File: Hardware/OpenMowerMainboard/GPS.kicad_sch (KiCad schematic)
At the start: 3 parts, among them U7 SIP32509DT

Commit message: added footprints to schematic
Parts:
- JP1: footprint (none) -> Jumper:SolderJumper-3_P1.3mm_Bridged12_Pad1.0x1.5mm
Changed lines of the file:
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@@
     (property "Reference" "JP1" (id 0) (at 212.09 113.03 0))
     (property "Value" "SolderJumper_3_Bridged12" (id 1) (at 212.09 115.57 0))
-    (property "Footprint" "" (id 2) (at 212.09 109.22 0)
+    (property "Footprint" "Jumper:SolderJumper-3_P1.3mm_Bridged12_Pad1.0x1.5mm" (id 2) (at 212.09 109.22 0)
       (effects (font (size 1.27 1.27)) hide)
     )

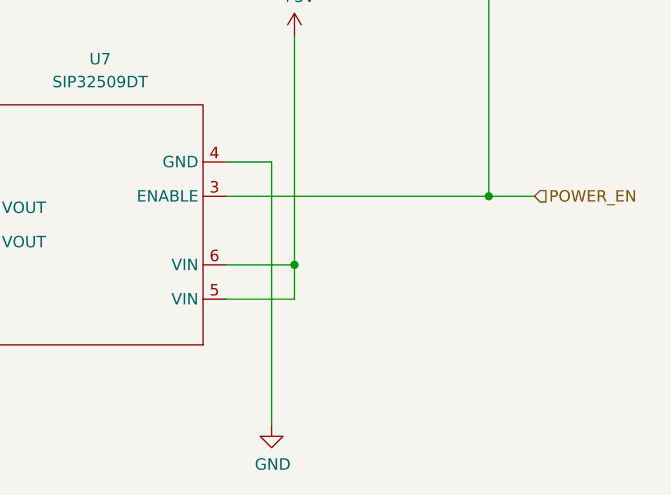
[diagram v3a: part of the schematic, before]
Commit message: Added default pull down, raspberry pi power override and some TODOs
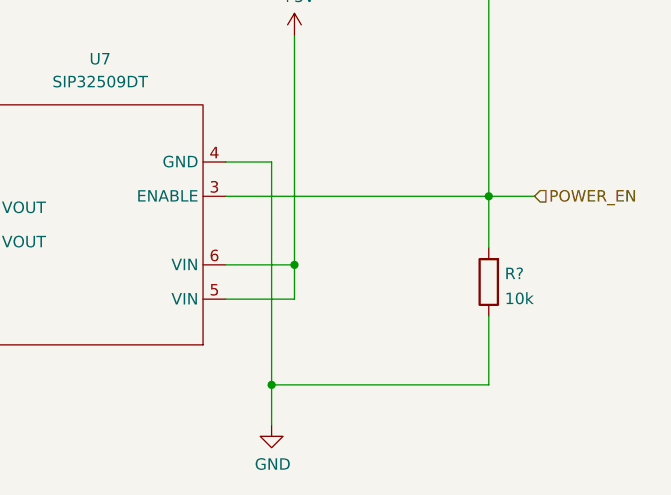
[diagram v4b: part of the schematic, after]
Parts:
- added R?: 10k, Resistor_SMD:R_0805_2012Metric_Pad1.20x1.40mm_HandSolder, symbol Device:R
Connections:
- net GND: now also R?.1
- net POWER_EN: now also R?.2
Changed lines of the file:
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@@
   (junction (at 118.11 93.98) (diameter 0) (color 0 0 0 0)
+  )
+  (junction (at 194.31 161.925) (diameter 0) (color 0 0 0 0)
   )
   (no_connect (at 121.92 83.82))
@@
     (stroke (width 0) (type default) (color 0 0 0 0))
   )
+  (wire (pts (xy 218.44 140.97) (xy 218.44 146.685))
+    (stroke (width 0) (type default) (color 0 0 0 0))
+  )
   (wire (pts (xy 201.93 109.22) (xy 207.01 109.22))
     (stroke (width 0) (type default) (color 0 0 0 0))
   )
+  (wire (pts (xy 218.44 154.305) (xy 218.44 161.925))
+    (stroke (width 0) (type default) (color 0 0 0 0))
+  )
   (wire (pts (xy 189.23 140.97) (xy 218.44 140.97))
     (stroke (width 0) (type default) (color 0 0 0 0))
@@
     (stroke (width 0) (type default) (color 0 0 0 0))
   )
+  (wire (pts (xy 218.44 161.925) (xy 194.31 161.925))
+    (stroke (width 0) (type default) (color 0 0 0 0))
+  )
   (wire (pts (xy 118.11 91.44) (xy 118.11 93.98))
     (stroke (width 0) (type default) (color 0 0 0 0))
@@
     (stroke (width 0) (type default) (color 0 0 0 0))
   )
-  (wire (pts (xy 194.31 137.16) (xy 194.31 166.37))
+  (wire (pts (xy 194.31 137.16) (xy 194.31 161.925))
     (stroke (width 0) (type default) (color 0 0 0 0))
   )
@@
   )
   (wire (pts (xy 187.96 104.14) (xy 212.09 104.14))
+    (stroke (width 0) (type default) (color 0 0 0 0))
+  )
+  (wire (pts (xy 194.31 161.925) (xy 194.31 166.37))
     (stroke (width 0) (type default) (color 0 0 0 0))
   )
@@
     (pin "3")
   )
+  (symbol (lib_id "Device:R") (at 218.44 150.495 180) (unit 1)
+    (in_bom yes) (on_board yes) (fields_autoplaced)
+    (property "Reference" "R?" (id 0) (at 220.218 149.5865 0)
+      (effects (font (size 1.27 1.27)) (justify right))
+    )
+    (property "Value" "10k" (id 1) (at 220.218 152.3616 0)
+      (effects (font (size 1.27 1.27)) (justify right))
+    )
+    (property "Footprint" "Resistor_SMD:R_0805_2012Metric_Pad1.20x1.40mm_HandSolder" (id 2) (at 220.218 150.495 90)
+      (effects (font (size 1.27 1.27)) hide)
+    )
+    (property "Datasheet" "~" (id 3) (at 218.44 150.495 0)
+      (effects (font (size 1.27 1.27)) hide)
+    )
+    (pin "1")
+    (pin "2")
+  )
   (symbol (lib_id "power:+3.3V") (at 201.93 109.22 0) (unit 1)

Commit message: WIP hardware revision
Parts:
- removed JP1: SolderJumper_3_Bridged12, Jumper:SolderJumper-3_P1.3mm_Bridged12_Pad1.0x1.5mm, symbol Jumper:SolderJumper_3_Bridged12
- removed R?: 10k, Resistor_SMD:R_0805_2012Metric_Pad1.20x1.40mm_HandSolder, symbol Device:R
- removed U7: SIP32509DT, Package_TO_SOT_SMD:SOT-23-6_Handsoldering, symbol OpenMowerMainboardLib:SIP32509DT
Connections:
- net GPS_POWER is gone; now on net +5V: XA1.5V1 (5V)
- net +3V3: now also XA1.IORF (IOREF)
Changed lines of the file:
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@@
 (kicad_sch (version 20211123) (generator eeschema)
   (paper "A4")
-  (junction (at 157.48 142.24) (diameter 0) (color 0 0 0 0)
-  )
-  (junction (at 218.44 140.97) (diameter 0) (color 0 0 0 0)
-  )
   (junction (at 118.11 96.52) (diameter 0) (color 0 0 0 0)
   )
-  (junction (at 196.85 148.59) (diameter 0) (color 0 0 0 0)
-  )
   (junction (at 118.11 93.98) (diameter 0) (color 0 0 0 0)
-  )
-  (junction (at 194.31 161.925) (diameter 0) (color 0 0 0 0)
   )
   (no_connect (at 121.92 83.82))
@@
     (stroke (width 0) (type default) (color 0 0 0 0))
   )
-  (wire (pts (xy 157.48 142.24) (xy 157.48 146.05))
-    (stroke (width 0) (type default) (color 0 0 0 0))
-  )
-  (wire (pts (xy 218.44 109.22) (xy 218.44 140.97))
-    (stroke (width 0) (type default) (color 0 0 0 0))
-  )
-  (wire (pts (xy 196.85 152.4) (xy 196.85 148.59))
-    (stroke (width 0) (type default) (color 0 0 0 0))
-  )
-  (wire (pts (xy 218.44 109.22) (xy 217.17 109.22))
-    (stroke (width 0) (type default) (color 0 0 0 0))
-  )
-  (wire (pts (xy 218.44 140.97) (xy 218.44 146.685))
-    (stroke (width 0) (type default) (color 0 0 0 0))
-  )
-  (wire (pts (xy 201.93 109.22) (xy 207.01 109.22))
-    (stroke (width 0) (type default) (color 0 0 0 0))
-  )
-  (wire (pts (xy 218.44 154.305) (xy 218.44 161.925))
-    (stroke (width 0) (type default) (color 0 0 0 0))
-  )
-  (wire (pts (xy 189.23 140.97) (xy 218.44 140.97))
-    (stroke (width 0) (type default) (color 0 0 0 0))
-  )
-  (wire (pts (xy 218.44 140.97) (xy 223.52 140.97))
-    (stroke (width 0) (type default) (color 0 0 0 0))
-  )
-  (wire (pts (xy 218.44 161.925) (xy 194.31 161.925))
-    (stroke (width 0) (type default) (color 0 0 0 0))
-  )
   (wire (pts (xy 118.11 91.44) (xy 118.11 93.98))
     (stroke (width 0) (type default) (color 0 0 0 0))
@@
     (stroke (width 0) (type default) (color 0 0 0 0))
   )
-  (wire (pts (xy 157.48 146.05) (xy 161.29 146.05))
+  (wire (pts (xy 96.52 98.425) (xy 96.52 101.6))
     (stroke (width 0) (type default) (color 0 0 0 0))
   )
-  (wire (pts (xy 157.48 142.24) (xy 161.29 142.24))
-    (stroke (width 0) (type default) (color 0 0 0 0))
-  )
-  (wire (pts (xy 99.06 101.6) (xy 121.92 101.6))
+  (wire (pts (xy 96.52 101.6) (xy 121.92 101.6))
     (stroke (width 0) (type default) (color 0 0 0 0))
   )
@@
     (stroke (width 0) (type default) (color 0 0 0 0))
   )
-  (wire (pts (xy 142.24 142.24) (xy 157.48 142.24))
-    (stroke (width 0) (type default) (color 0 0 0 0))
-  )
-  (wire (pts (xy 212.09 104.14) (xy 212.09 105.41))
-    (stroke (width 0) (type default) (color 0 0 0 0))
-  )
   (wire (pts (xy 121.92 91.44) (xy 118.11 91.44))
-    (stroke (width 0) (type default) (color 0 0 0 0))
-  )
-  (wire (pts (xy 189.23 152.4) (xy 196.85 152.4))
     (stroke (width 0) (type default) (color 0 0 0 0))
   )
@@
     (stroke (width 0) (type default) (color 0 0 0 0))
   )
-  (wire (pts (xy 196.85 123.19) (xy 196.85 148.59))
-    (stroke (width 0) (type default) (color 0 0 0 0))
-  )
-  (wire (pts (xy 194.31 137.16) (xy 194.31 161.925))
-    (stroke (width 0) (type default) (color 0 0 0 0))
-  )
-  (wire (pts (xy 189.23 148.59) (xy 196.85 148.59))
-    (stroke (width 0) (type default) (color 0 0 0 0))
-  )
-  (wire (pts (xy 189.23 137.16) (xy 194.31 137.16))
-    (stroke (width 0) (type default) (color 0 0 0 0))
-  )
-  (wire (pts (xy 187.96 104.14) (xy 212.09 104.14))
-    (stroke (width 0) (type default) (color 0 0 0 0))
-  )
-  (wire (pts (xy 194.31 161.925) (xy 194.31 166.37))
+  (wire (pts (xy 187.96 104.14) (xy 196.85 104.14))
     (stroke (width 0) (type default) (color 0 0 0 0))
   )
@@
     (effects (font (size 1.27 1.27)) (justify left bottom))
   )
-  (label "GPS_POWER" (at 142.24 142.24 0)
-    (effects (font (size 1.27 1.27)) (justify left bottom))
-  )
   (hierarchical_label "TXD" (shape output) (at 121.92 50.8 180)
     (effects (font (size 1.27 1.27)) (justify right))
-  )
-  (hierarchical_label "POWER_EN" (shape input) (at 223.52 140.97 0)
-    (effects (font (size 1.27 1.27)) (justify left))
   )
   (hierarchical_label "RXD" (shape input) (at 121.92 53.34 180)
@@
     (pin "VIN")
   )
-  (symbol (lib_id "Jumper:SolderJumper_3_Bridged12") (at 212.09 109.22 180) (unit 1)
+  (symbol (lib_id "power:+3.3V") (at 196.85 104.14 0) (unit 1)
     (in_bom yes) (on_board yes) (fields_autoplaced)
-    (property "Reference" "JP1" (id 0) (at 212.09 113.03 0))
-    (property "Value" "SolderJumper_3_Bridged12" (id 1) (at 212.09 115.57 0))
-    (property "Footprint" "Jumper:SolderJumper-3_P1.3mm_Bridged12_Pad1.0x1.5mm" (id 2) (at 212.09 109.22 0)
+    (property "Reference" "#PWR0116" (id 0) (at 196.85 107.95 0)
       (effects (font (size 1.27 1.27)) hide)
     )
-    (property "Datasheet" "~" (id 3) (at 212.09 109.22 0)
+    (property "Value" "+3.3V" (id 1) (at 196.85 99.06 0))
+    (property "Footprint" "" (id 2) (at 196.85 104.14 0)
       (effects (font (size 1.27 1.27)) hide)
     )
-    (pin "1")
-    (pin "2")
-    (pin "3")
-  )
-  (symbol (lib_id "Device:R") (at 218.44 150.495 180) (unit 1)
-    (in_bom yes) (on_board yes) (fields_autoplaced)
-    (property "Reference" "R?" (id 0) (at 220.218 149.5865 0)
-      (effects (font (size 1.27 1.27)) (justify right))
-    )
-    (property "Value" "10k" (id 1) (at 220.218 152.3616 0)
-      (effects (font (size 1.27 1.27)) (justify right))
-    )
-    (property "Footprint" "Resistor_SMD:R_0805_2012Metric_Pad1.20x1.40mm_HandSolder" (id 2) (at 220.218 150.495 90)
-      (effects (font (size 1.27 1.27)) hide)
-    )
-    (property "Datasheet" "~" (id 3) (at 218.44 150.495 0)
-      (effects (font (size 1.27 1.27)) hide)
-    )
-    (pin "1")
-    (pin "2")
-  )
-  (symbol (lib_id "power:+3.3V") (at 201.93 109.22 0) (unit 1)
-    (in_bom yes) (on_board yes) (fields_autoplaced)
-    (property "Reference" "#PWR0116" (id 0) (at 201.93 113.03 0)
-      (effects (font (size 1.27 1.27)) hide)
-    )
-    (property "Value" "+3.3V" (id 1) (at 201.93 104.14 0))
-    (property "Footprint" "" (id 2) (at 201.93 109.22 0)
-      (effects (font (size 1.27 1.27)) hide)
-    )
-    (property "Datasheet" "" (id 3) (at 201.93 109.22 0)
+    (property "Datasheet" "" (id 3) (at 196.85 104.14 0)
       (effects (font (size 1.27 1.27)) hide)
     )
     (pin "1")
   )
-  (symbol (lib_id "OpenMowerMainboardLib:SIP32509DT") (at 163.83 116.84 180) (unit 1)
-    (in_bom yes) (on_board yes) (fields_autoplaced)
-    (property "Reference" "U7" (id 0) (at 175.26 125.73 0))
-    (property "Value" "SIP32509DT" (id 1) (at 175.26 128.27 0))
-    (property "Footprint" "Package_TO_SOT_SMD:SOT-23-6_Handsoldering" (id 2) (at 163.83 116.84 0)
+  (symbol (lib_id "power:+5V") (at 96.52 98.425 0) (unit 1)
+    (in_bom yes) (on_board yes)
+    (property "Reference" "#PWR0134" (id 0) (at 96.52 102.235 0)
       (effects (font (size 1.27 1.27)) hide)
     )
-    (property "Datasheet" "" (id 3) (at 163.83 116.84 0)
+    (property "Value" "+5V" (id 1) (at 96.901 94.0308 0))
+    (property "Footprint" "" (id 2) (at 96.52 98.425 0)
       (effects (font (size 1.27 1.27)) hide)
     )
-    (pin "1")
-    (pin "2")
-    (pin "3")
-    (pin "4")
-    (pin "5")
-    (pin "6")
-  )
-  (symbol (lib_id "power:+5V") (at 196.85 123.19 0) (unit 1)
-    (in_bom yes) (on_board yes)
-    (property "Reference" "#PWR0134" (id 0) (at 196.85 127 0)
+    (property "Datasheet" "" (id 3) (at 96.52 98.425 0)
       (effects (font (size 1.27 1.27)) hide)
     )
-    (property "Value" "+5V" (id 1) (at 197.231 118.7958 0))
-    (property "Footprint" "" (id 2) (at 196.85 123.19 0)
-      (effects (font (size 1.27 1.27)) hide)
-    )
-    (property "Datasheet" "" (id 3) (at 196.85 123.19 0)
-      (effects (font (size 1.27 1.27)) hide)
-    )
-    (pin "1")
-  )
-  (symbol (lib_id "power:GND") (at 194.31 166.37 0) (unit 1)
-    (in_bom yes) (on_board yes)
-    (property "Reference" "#PWR0133" (id 0) (at 194.31 172.72 0)
-      (effects (font (size 1.27 1.27)) hide)
-    )
-    (property "Value" "GND" (id 1) (at 194.437 170.7642 0))
-    (property "Footprint" "" (id 2) (at 194.31 166.37 0)
-      (effects (font (size 1.27 1.27)) hide)
-    )
-    (property "Datasheet" "" (id 3) (at 194.31 166.37 0)
-      (effects (font (size 1.27 1.27)) hide)
-    )

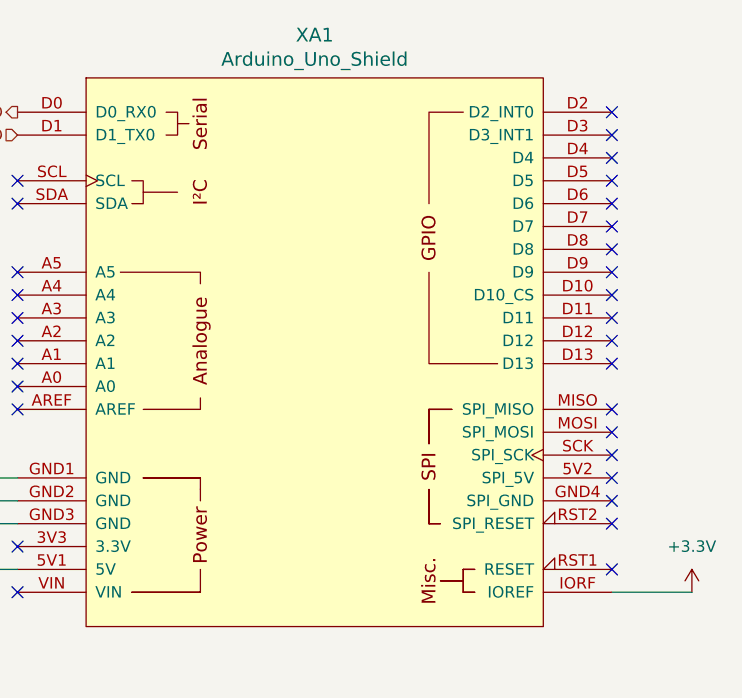
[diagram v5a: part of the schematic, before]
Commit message: v0_9_1 mainboard rework
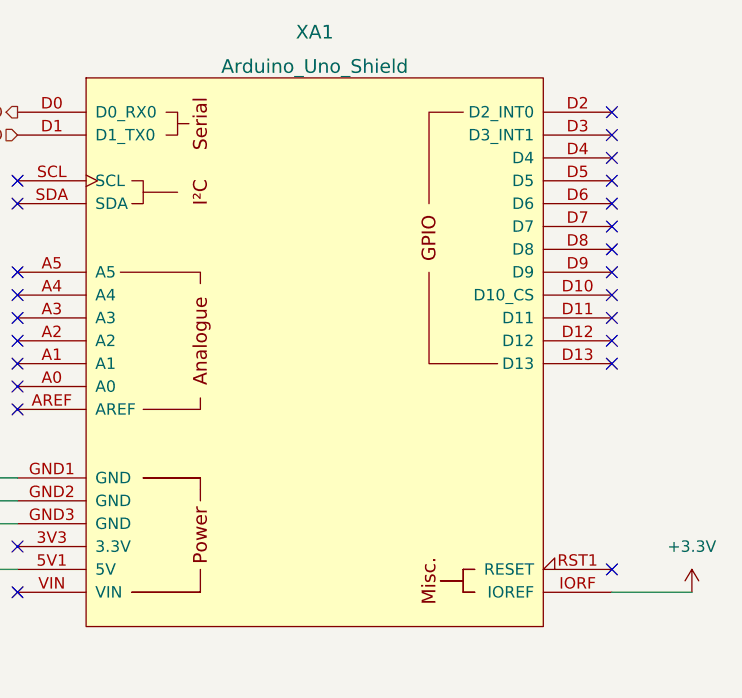
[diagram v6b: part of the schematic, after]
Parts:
- removed XA1: Arduino_Uno_Shield, Arduino:Arduino_Uno_Shield, symbol arduino:Arduino_Uno_Shield
- added XA1: Arduino_Uno_Shield, MyModules:Arduino_Uno_Shield, symbol MyModules:Arduino_Uno_Shield
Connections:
- net +3V3: now also XA1.IORF (IOREF)
- net +5V: now also XA1.5V1 (5V)
- net GND: now also XA1.GND1 (GND), XA1.GND2 (GND), XA1.GND3 (GND)
- net RXD: now also XA1.D1 (D1_TX0)
- net TXD: now also XA1.D0 (D0_RX0)
- no-connect marks 30 -> 24
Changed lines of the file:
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@@
   (no_connect (at 187.96 76.2))
   (no_connect (at 187.96 78.74))
-  (no_connect (at 187.96 83.82))
-  (no_connect (at 187.96 86.36))
-  (no_connect (at 187.96 88.9))
   (no_connect (at 187.96 63.5))
   (no_connect (at 187.96 66.04))
@@
   (no_connect (at 187.96 60.96))
   (no_connect (at 187.96 101.6))
-  (no_connect (at 187.96 96.52))
-  (no_connect (at 187.96 93.98))
-  (no_connect (at 187.96 91.44))
   (no_connect (at 121.92 99.06))
   (no_connect (at 121.92 104.14))
@@
     (pin "1")
   )
-  (symbol (lib_id "arduino:Arduino_Uno_Shield") (at 154.94 77.47 0) (unit 1)
-    (in_bom yes) (on_board yes)
-    (property "Reference" "XA1" (id 0) (at 154.94 42.2402 0)
-      (effects (font (size 1.524 1.524)))
-    )
-    (property "Value" "Arduino_Uno_Shield" (id 1) (at 154.94 44.9326 0)
-      (effects (font (size 1.524 1.524)))
-    )
-    (property "Footprint" "Arduino:Arduino_Uno_Shield" (id 2) (at 200.66 -17.78 0)
-      (effects (font (size 1.524 1.524)) hide)
-    )
-    (property "Datasheet" "" (id 3) (at 200.66 -17.78 0)
-      (effects (font (size 1.524 1.524)) hide)
-    )
-    (pin "3V3")
-    (pin "5V1")
-    (pin "5V2")
-    (pin "A0")
-    (pin "A1")
-    (pin "A2")
-    (pin "A3")
-    (pin "A4")
-    (pin "A5")
-    (pin "AREF")
-    (pin "D0")
-    (pin "D1")
-    (pin "D10")
-    (pin "D11")
-    (pin "D12")
-    (pin "D13")
-    (pin "D2")
-    (pin "D3")
-    (pin "D4")
-    (pin "D5")
-    (pin "D6")
-    (pin "D7")
-    (pin "D8")
-    (pin "D9")
-    (pin "GND1")
-    (pin "GND2")
-    (pin "GND3")
-    (pin "GND4")
-    (pin "IORF")
-    (pin "MISO")
-    (pin "MOSI")
-    (pin "RST1")
-    (pin "RST2")
-    (pin "SCK")
-    (pin "SCL")
-    (pin "SDA")
-    (pin "VIN")
-  )
   (symbol (lib_id "power:+3.3V") (at 196.85 104.14 0) (unit 1)
     (in_bom yes) (on_board yes) (fields_autoplaced)
@@
     (pin "1")
   )
+  (symbol (lib_id "MyModules:Arduino_Uno_Shield") (at 154.94 77.47 0) (unit 1)
+    (in_bom yes) (on_board yes) (fields_autoplaced)
+    (property "Reference" "XA1" (id 0) (at 154.94 41.91 0)
+      (effects (font (size 1.524 1.524)))
+    )
+    (property "Value" "Arduino_Uno_Shield" (id 1) (at 154.94 45.72 0)
+      (effects (font (size 1.524 1.524)))
+    )
+    (property "Footprint" "MyModules:Arduino_Uno_Shield" (id 2) (at 200.66 -17.78 0)
+      (effects (font (size 1.524 1.524)) hide)
+    )
+    (property "Datasheet" "" (id 3) (at 200.66 -17.78 0)
+      (effects (font (size 1.524 1.524)) hide)
+    )
+    (pin "3V3")
+    (pin "5V1")
+    (pin "A0")
+    (pin "A1")
+    (pin "A2")
+    (pin "A3")
+    (pin "A4")
+    (pin "A5")
+    (pin "AREF")
+    (pin "D0")
+    (pin "D1")
+    (pin "D10")
+    (pin "D11")
+    (pin "D12")
+    (pin "D13")
+    (pin "D2")
+    (pin "D3")
+    (pin "D4")
+    (pin "D5")
+    (pin "D6")
+    (pin "D7")
+    (pin "D8")
+    (pin "D9")
+    (pin "GND1")
+    (pin "GND2")
+    (pin "GND3")
+    (pin "IORF")
+    (pin "RST1")
+    (pin "SCL")
+    (pin "SDA")
+    (pin "VIN")
+  )
 )
